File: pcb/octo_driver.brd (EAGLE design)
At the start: 34.3 x 46.2 mm, 16 parts

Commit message: Bottom layer silkscreen
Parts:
- added E$2: (no value), penrose:PENROSELOGO_1.75IN
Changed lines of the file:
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@@
 <layer number="24" name="bOrigins" color="15" fill="1" visible="yes" active="yes"/>
 <layer number="25" name="tNames" color="7" fill="1" visible="yes" active="yes"/>
-<layer number="26" name="bNames" color="7" fill="1" visible="yes" active="yes"/>
+<layer number="26" name="bNames" color="7" fill="1" visible="no" active="yes"/>
 <layer number="27" name="tValues" color="7" fill="1" visible="yes" active="yes"/>
 <layer number="28" name="bValues" color="7" fill="1" visible="yes" active="yes"/>
@@
 <element name="H3" library="holes" package="2,8-PAD" value="MOUNT-PAD-ROUND2.8" x="72.644" y="49.784"/>
 <element name="E$1" library="penrose" package="PENROSELOGO_LOWDPI" value="" x="54.102" y="48.26"/>
+<element name="E$2" library="penrose" package="PENROSELOGO_1.75IN" value="" x="68.326" y="26.924"/>
 </elements>
 <signals>

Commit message: Crop bottom silkscreen to board outline, just in case
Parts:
- moved E$2 17.5 mm to (50.8, 27.4)
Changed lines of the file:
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@@
 <element name="H3" library="holes" package="2,8-PAD" value="MOUNT-PAD-ROUND2.8" x="72.644" y="49.784"/>
 <element name="E$1" library="penrose" package="PENROSELOGO_LOWDPI" value="" x="54.102" y="48.26"/>
-<element name="E$2" library="penrose" package="PENROSELOGO_1.75IN" value="" x="68.326" y="26.924"/>
+<element name="E$2" library="penrose" package="PENROSELOGO_1.75IN" value="" x="50.8" y="27.432"/>
 </elements>
 <signals>

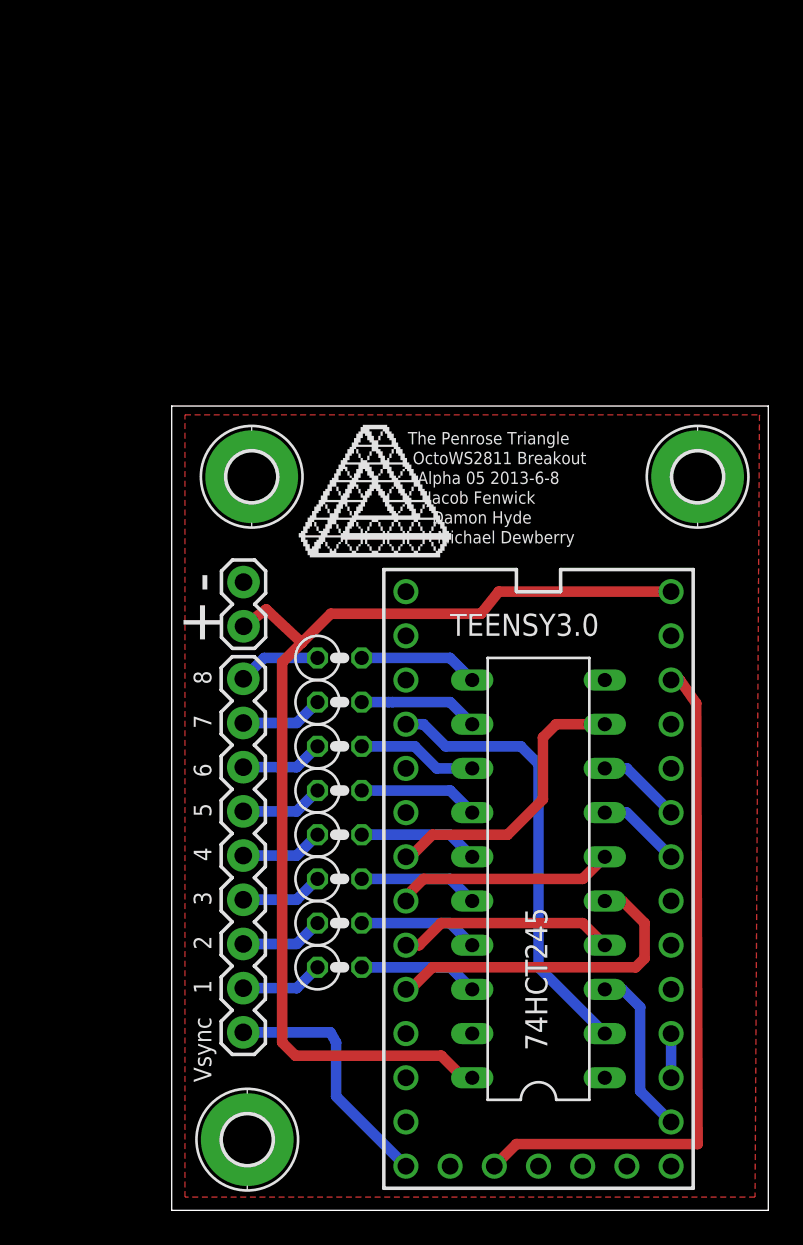
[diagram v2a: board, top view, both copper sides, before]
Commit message: modified damon's board to have art, added missing trace
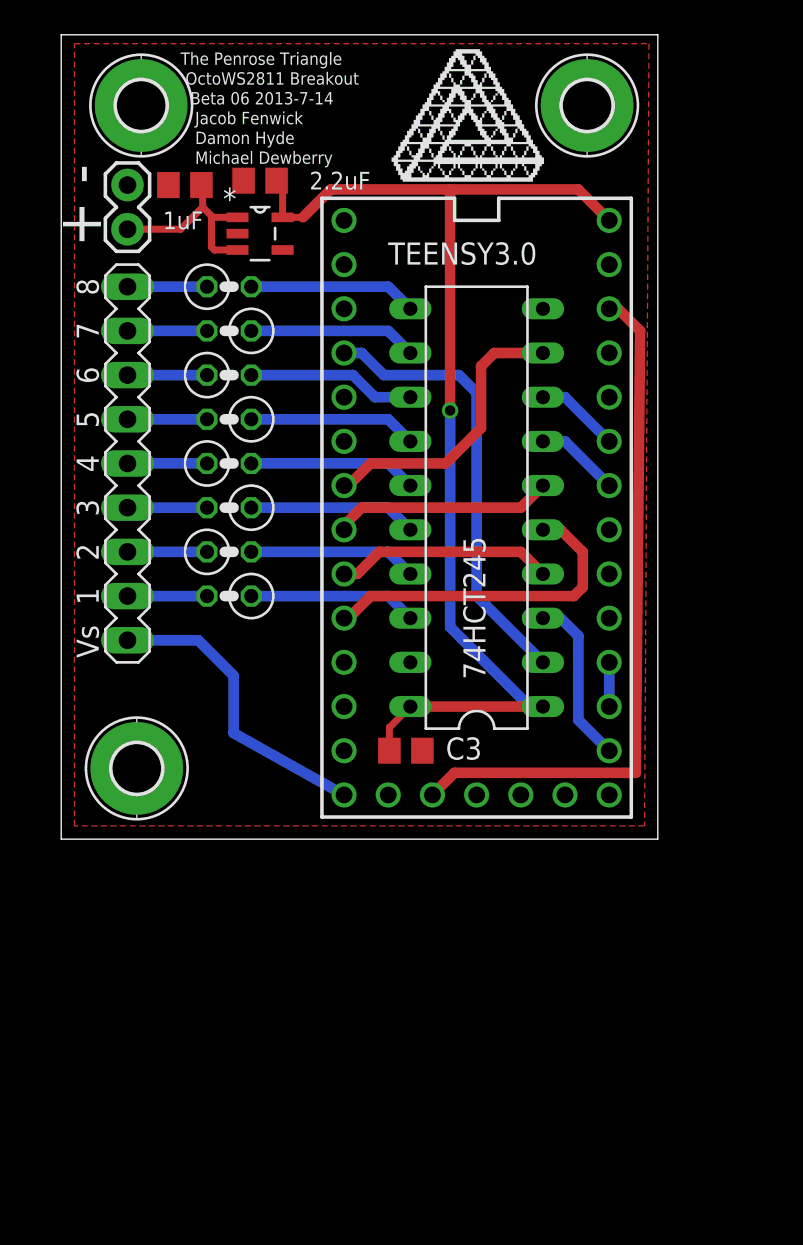
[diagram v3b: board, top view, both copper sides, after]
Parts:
- removed E$1: (no value), penrose:PENROSELOGO_LOWDPI
- removed E$2: (no value), penrose:PENROSELOGO_1.75IN
- removed JP3: M09, SparkFun-Connectors:1X09
- added C1: 2.2uF, rcl:C0805
- added C2: 1uF, rcl:C0805
- added C3: (no value), rcl:C0805
- added SV1: (no value), penrose-con-lstb:MA09-1
- added U$1: (no value), penrose:PENROSELOGO_LOWDPI
- added U$2: (no value), penrose:PENROSELOGO_1.75IN
- added U1: LP2985-10DBVT, Texas Instruments_By_element14_Batch_1:SOT95P280X145-5N
- moved JP1 23.8 mm to (39.9, 66.5)
- moved H3 22.3 mm to (66.3, 71.1)
- moved H1 22.3 mm to (40.4, 33.0)
- moved H2 22.3 mm to (40.7, 71.1)
- moved RLED1 22.3 mm to (45.7, 60.7)
- moved RLED13 22.3 mm to (45.7, 45.5)
- moved RLED14 22.3 mm to (45.7, 42.9), turned to 180 degrees
- moved RLED10 22.3 mm to (45.7, 53.1), turned to 180 degrees
- moved RLED11 22.3 mm to (45.7, 50.5)
- moved RLED12 22.3 mm to (45.7, 48.0), turned to 180 degrees
- moved RLED8 22.3 mm to (45.7, 58.2), turned to 180 degrees
- moved RLED9 22.3 mm to (45.7, 55.6)
- moved 74HCT245 21.6 mm to (59.9, 48.0)
- moved TEENSY3.0 21.6 mm to (59.9, 48.0)
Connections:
- net N$2 renamed LED7_3.3
- net N$26 renamed LED8_3.3
- net N$4 renamed LED2_3.3
- net N$5 renamed LED3_3.3
- net N$6 renamed LED4_3.3
- net N$7 renamed LED5_3.3
- net N$9 renamed LED6_3.3
- removed net +5V: 74HCT245.20, JP1.2, TEENSY3.0.VIN
- removed net N$10: JP3.7, RLED9.1
- removed net N$11: JP3.6, RLED10.1
- removed net N$12: JP3.5, RLED11.1
- removed net N$13: JP3.4, RLED12.1
- removed net N$14: JP3.3, RLED13.1
- removed net N$15: JP3.2, RLED14.1
- removed net N$8: JP3.8, RLED8.1
- new net LED1_3.3: 74HCT245.2, TEENSY3.0.2
- new net LED2: RLED13.1, SV1.3
- new net LED3: RLED12.2, SV1.4
- new net LED4: RLED11.1, SV1.5
- new net LED5: RLED10.2, SV1.6
- new net LED6: RLED9.1, SV1.7
- new net LED7: RLED8.2, SV1.8
- new net LED8: RLED1.1, SV1.9
- new net VCC: 74HCT245.1, 74HCT245.20, C1.1, C3.1, TEENSY3.0.VIN, U1.5
- net GND: now also C1.2, C2.1, C3.2, H1.B2,8, U1.2
- net LED1: now also RLED14.2, SV1.2; no longer 74HCT245.2, TEENSY3.0.2
- net N$1: now also C2.2, JP1.2, U1.1, U1.3; no longer JP3.9, RLED1.1
- net N$17: now also RLED8.1; no longer RLED8.2
- net N$20: now also RLED10.1; no longer RLED10.2
- net N$22: now also RLED12.1; no longer RLED12.2
- net N$24: now also RLED14.1; no longer RLED14.2
- net VSYNC: now also SV1.1; no longer JP3.1
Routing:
- net VCC: track 0.00 -> 65.5 mm, vias 0 -> 1
- net +5V: track 62.2 -> 0.00 mm
- net LED1_3.3: track 0.00 -> 25.6 mm
- net LED1: track 25.6 -> 4.57 mm
- net N$1: track 4.76 -> 11.7 mm
- net N$13: track 4.76 -> 0.00 mm
- net N$8: track 4.76 -> 0.00 mm
- net N$15: track 4.76 -> 0.00 mm
- net N$14: track 4.76 -> 0.00 mm
- net N$12: track 4.76 -> 0.00 mm
- net N$11: track 4.76 -> 0.00 mm
- net N$10: track 4.76 -> 0.00 mm
- net LED8: track 0.00 -> 4.57 mm
- net LED7: track 0.00 -> 4.57 mm
- net LED6: track 0.00 -> 4.57 mm
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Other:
- board text added: "+ -"
- board text added: "The Penrose Triangle OctoWS2811 Breakout Beta 06 2013-7-14 Jacob Fenwick Damon Hyde Michael Dewberry"
- board text removed: "+"
- board text removed: "-"
- board text removed: "1"
- board text removed: "2"
- board text removed: "3"
- board text removed: "4"
- board text removed: "5"
- board text removed: "6"
- board text removed: "7"
- board text removed: "8"
- board text removed: "The Penrose Triangle OctoWS2811 Breakout Alpha 05 2013-6-8 Jacob Fenwick Damon Hyde Michael Dewberry"
- board text removed: "Vsync"

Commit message: removed unnecessary trace connecting the 3.3v pins on the teensy
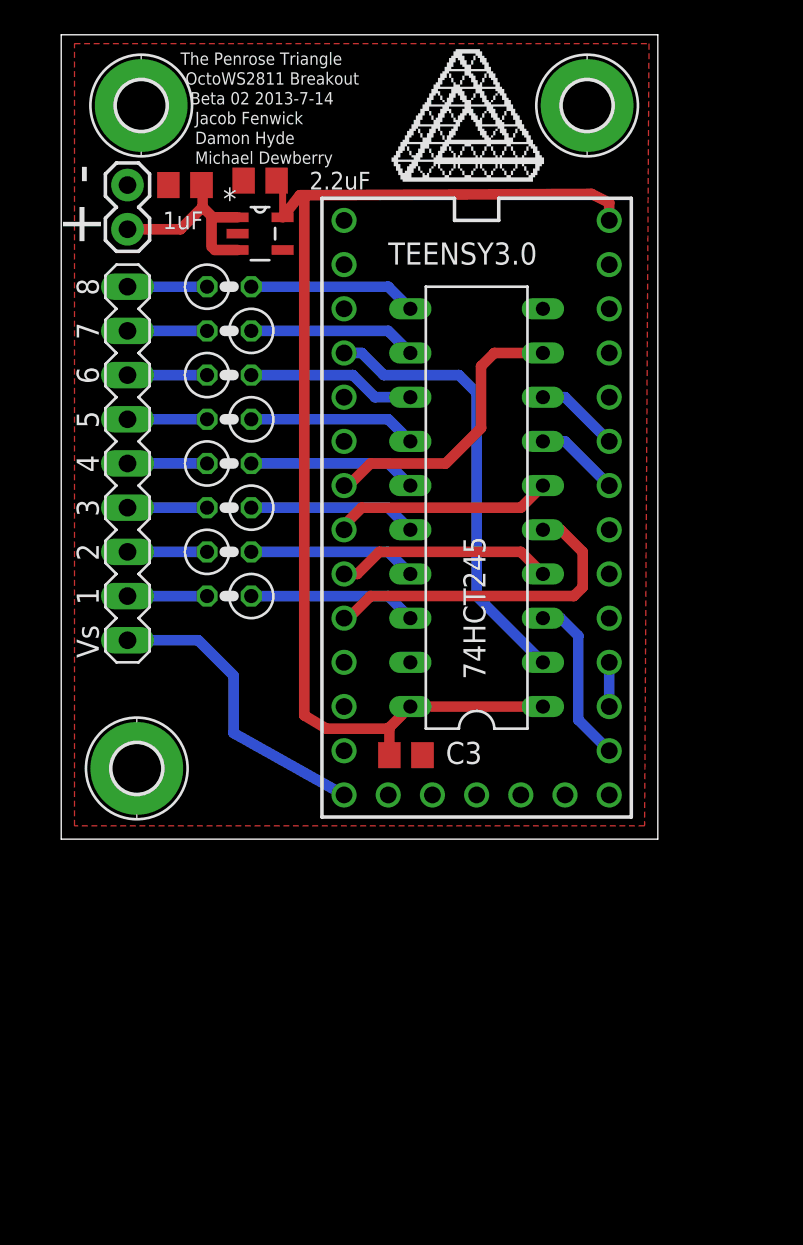
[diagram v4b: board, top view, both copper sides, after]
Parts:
- moved C3 0.25 mm to (55.9, 33.8)
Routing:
- net 3.3V: track 39.9 -> 0.00 mm
- net VCC: track 65.5 -> 68.4 mm, vias 1 -> 0
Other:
- board text added: "The Penrose Triangle OctoWS2811 Breakout Beta 02 2013-7-14 Jacob Fenwick Damon Hyde Michael Dewberry"
- board text removed: "The Penrose Triangle OctoWS2811 Breakout Beta 06 2013-7-14 Jacob Fenwick Damon Hyde Michael Dewberry"
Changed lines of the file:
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@@
 <text x="42.926" y="74.168" size="0.7112" layer="25" font="vector" ratio="15" distance="60" align="top-left">The Penrose Triangle
  OctoWS2811 Breakout
-  Beta 06 2013-7-14
+  Beta 02 2013-7-14
    Jacob Fenwick
    Damon Hyde
@@
 <element name="H2" library="holes" package="2,8-PAD" value="MOUNT-PAD-ROUND2.8" x="40.666" y="71.12"/>
 <element name="H3" library="holes" package="2,8-PAD" value="MOUNT-PAD-ROUND2.8" x="66.294" y="71.12"/>
-<element name="C3" library="rcl" package="C0805" value="" x="55.88" y="34.036" smashed="yes">
-<attribute name="NAME" x="58.166" y="33.528" size="1.27" layer="25"/>
-<attribute name="VALUE" x="54.61" y="31.496" size="1.27" layer="27"/>
+<element name="C3" library="rcl" package="C0805" value="" x="55.88" y="33.782" smashed="yes">
+<attribute name="NAME" x="58.166" y="33.274" size="1.27" layer="25"/>
+<attribute name="VALUE" x="54.61" y="31.242" size="1.27" layer="27"/>
 </element>
 <element name="SV1" library="penrose-con-lstb" package="MA09-1" value="" x="39.878" y="50.546" smashed="yes" rot="R90">
@@
 <contactref element="TEENSY3.0" pad="3.3V1"/>
 <contactref element="TEENSY3.0" pad="3.3V"/>
-<wire x1="67.564" y1="59.436" x2="68.072" y2="59.436" width="0.6096" layer="1"/>
-<wire x1="68.072" y1="59.436" x2="69.342" y2="58.166" width="0.6096" layer="1"/>
-<wire x1="69.342" y1="58.166" x2="69.088" y2="32.766" width="0.6096" layer="1"/>
-<wire x1="69.088" y1="32.766" x2="58.674" y2="32.766" width="0.6096" layer="1"/>
-<wire x1="58.674" y1="32.766" x2="57.404" y2="31.496" width="0.6096" layer="1"/>
+<wire x1="57.404" y1="31.496" x2="67.564" y2="59.436" width="0" layer="19" extent="1-1"/>
 </signal>
 <signal name="LED2">
@@
 <contactref element="U1" pad="3"/>
 <contactref element="C2" pad="2"/>
-<wire x1="39.878" y1="64.008" x2="42.926" y2="64.008" width="0.4064" layer="1"/>
-<wire x1="42.926" y1="64.008" x2="44.196" y2="65.278" width="0.4064" layer="1"/>
-<wire x1="44.196" y1="65.278" x2="44.196" y2="66.482" width="0.4064" layer="1"/>
+<wire x1="39.878" y1="64.008" x2="42.926" y2="64.008" width="0.6096" layer="1"/>
+<wire x1="42.926" y1="64.008" x2="44.196" y2="65.278" width="0.6096" layer="1"/>
+<wire x1="44.196" y1="65.278" x2="44.196" y2="66.482" width="0.6096" layer="1"/>
 <wire x1="44.196" y1="66.482" x2="44.13" y2="66.548" width="0.4064" layer="1"/>
-<wire x1="46.2026" y1="64.6938" x2="44.7802" y2="64.6938" width="0.4064" layer="1"/>
-<wire x1="44.7802" y1="64.6938" x2="44.196" y2="65.278" width="0.4064" layer="1"/>
-<wire x1="46.2026" y1="62.8142" x2="44.8818" y2="62.8142" width="0.4064" layer="1"/>
+<wire x1="46.2026" y1="64.6938" x2="44.7802" y2="64.6938" width="0.6096" layer="1"/>
+<wire x1="44.7802" y1="64.6938" x2="44.196" y2="65.278" width="0.6096" layer="1"/>
+<wire x1="46.2026" y1="62.8142" x2="44.8818" y2="62.8142" width="0.6096" layer="1"/>
 <wire x1="44.8818" y1="62.8142" x2="44.704" y2="62.992" width="0.4064" layer="1"/>
-<wire x1="44.704" y1="62.992" x2="44.704" y2="64.6176" width="0.4064" layer="1"/>
+<wire x1="44.704" y1="62.992" x2="44.704" y2="64.6176" width="0.6096" layer="1"/>
 <wire x1="44.704" y1="64.6176" x2="44.7802" y2="64.6938" width="0.4064" layer="1"/>
 </signal>
@@
 <contactref element="74HCT245" pad="20"/>
 <contactref element="C3" pad="1"/>
-<wire x1="54.93" y1="34.036" x2="54.93" y2="35.372" width="0.4064" layer="1"/>
-<wire x1="54.93" y1="35.372" x2="56.134" y2="36.576" width="0.4064" layer="1"/>
-<wire x1="49.9618" y1="64.6938" x2="51.562" y2="66.294" width="0.6096" layer="1"/>
-<wire x1="51.562" y1="66.294" x2="58.42" y2="66.294" width="0.6096" layer="1"/>
-<wire x1="58.42" y1="66.294" x2="65.786" y2="66.294" width="0.6096" layer="1"/>
-<wire x1="65.786" y1="66.294" x2="67.564" y2="64.516" width="0.6096" layer="1"/>
+<wire x1="54.93" y1="33.782" x2="54.93" y2="35.372" width="0.6096" layer="1"/>
+<wire x1="54.93" y1="35.372" x2="56.134" y2="36.576" width="0.6096" layer="1"/>
 <wire x1="63.754" y1="36.576" x2="56.134" y2="36.576" width="0.6096" layer="1"/>
-<wire x1="63.754" y1="36.576" x2="62.992" y2="36.576" width="0.6096" layer="16"/>
-<wire x1="62.992" y1="36.576" x2="58.42" y2="41.148" width="0.6096" layer="16"/>
-<wire x1="58.42" y1="41.148" x2="58.42" y2="53.594" width="0.6096" layer="16"/>
-<via x="58.42" y="53.594" extent="1-16" drill="0.6" shape="square"/>
-<wire x1="58.42" y1="53.594" x2="58.42" y2="66.294" width="0.6096" layer="1"/>
 <contactref element="U1" pad="5"/>
 <contactref element="C1" pad="1"/>
 <wire x1="48.7934" y1="64.6938" x2="48.7934" y2="66.4566" width="0.4064" layer="1"/>
 <wire x1="48.7934" y1="66.4566" x2="48.448" y2="66.802" width="0.4064" layer="1"/>
-<wire x1="49.9618" y1="64.6938" x2="48.7934" y2="64.6938" width="0.4064" layer="1"/>
+<wire x1="48.7934" y1="64.6938" x2="49.784" y2="65.9638" width="0.6096" layer="1"/>
+<wire x1="49.784" y1="65.9638" x2="66.548" y2="66.04" width="0.6096" layer="1"/>
+<wire x1="66.548" y1="66.04" x2="67.564" y2="65.532" width="0.6096" layer="1"/>
+<wire x1="67.564" y1="65.532" x2="67.564" y2="64.516" width="0.6096" layer="1"/>
+<wire x1="51.308" y1="35.306" x2="50.038" y2="36.068" width="0.6096" layer="1"/>
+<wire x1="50.038" y1="36.068" x2="50.038" y2="65.786" width="0.6096" layer="1"/>
+<wire x1="51.308" y1="35.306" x2="54.864" y2="35.306" width="0.6096" layer="1"/>
+<wire x1="50.038" y1="65.786" x2="49.784" y2="65.9638" width="0" layer="19" extent="1-1"/>
+<wire x1="54.93" y1="35.372" x2="54.864" y2="35.306" width="0" layer="19" extent="1-1"/>
 </signal>
 </signals>

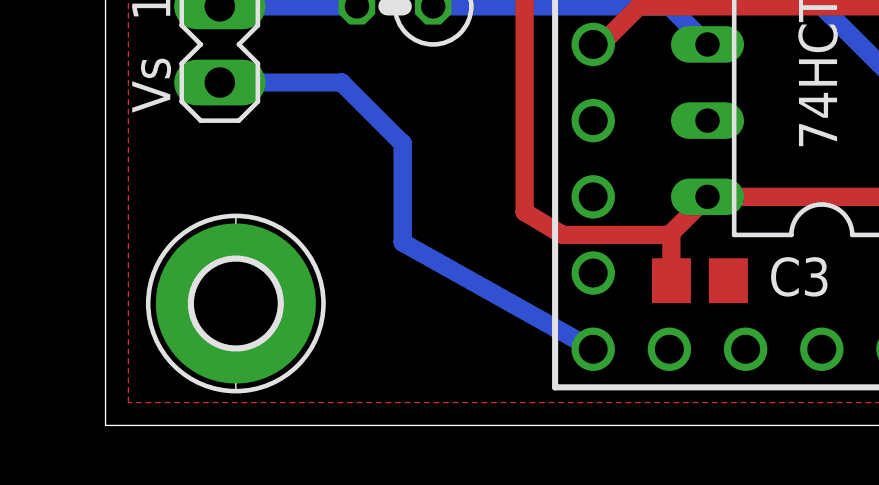
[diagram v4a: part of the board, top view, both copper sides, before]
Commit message: added test pin for connecting a scope or multimeter
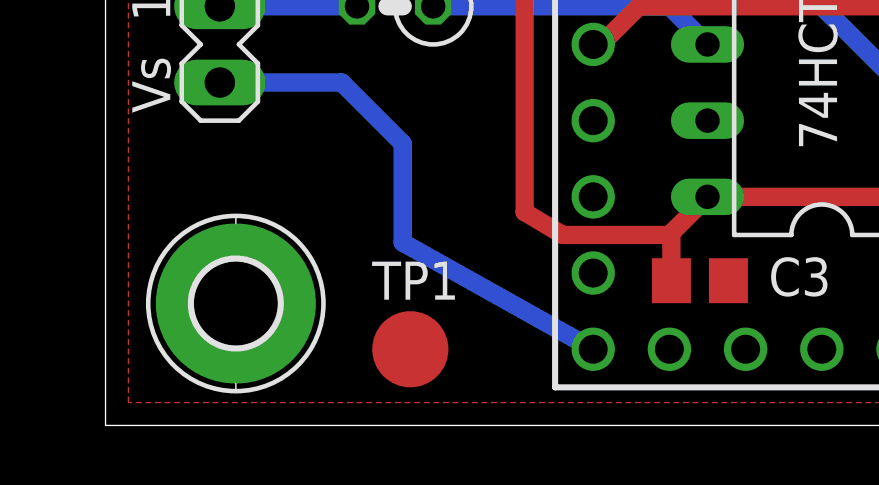
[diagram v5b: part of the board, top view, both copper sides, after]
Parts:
- added TP1: PTR1B2,54, testpad:B2,54
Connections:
- net GND: now also TP1.TP
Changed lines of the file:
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@@
 <element name="U$1" library="penrose" package="PENROSELOGO_LOWDPI" value="" x="59.436" y="69.85"/>
 <element name="U$2" library="penrose" package="PENROSELOGO_1.75IN" value="" x="44.196" y="49.276"/>
+<element name="TP1" library="testpad" package="B2,54" value="PTR1B2,54" x="46.228" y="31.496">
+<attribute name="TP_SIGNAL_NAME" value="" x="46.228" y="31.496" size="1.778" layer="27" display="off"/>
+</element>
 </elements>
 <signals>
@@
 <contactref element="C2" pad="1"/>
 <contactref element="C1" pad="2"/>
+<contactref element="TP1" pad="TP"/>
 </signal>
 <signal name="N$16">
